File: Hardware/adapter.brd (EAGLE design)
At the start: 61.9 x 62.5 mm, 6 parts

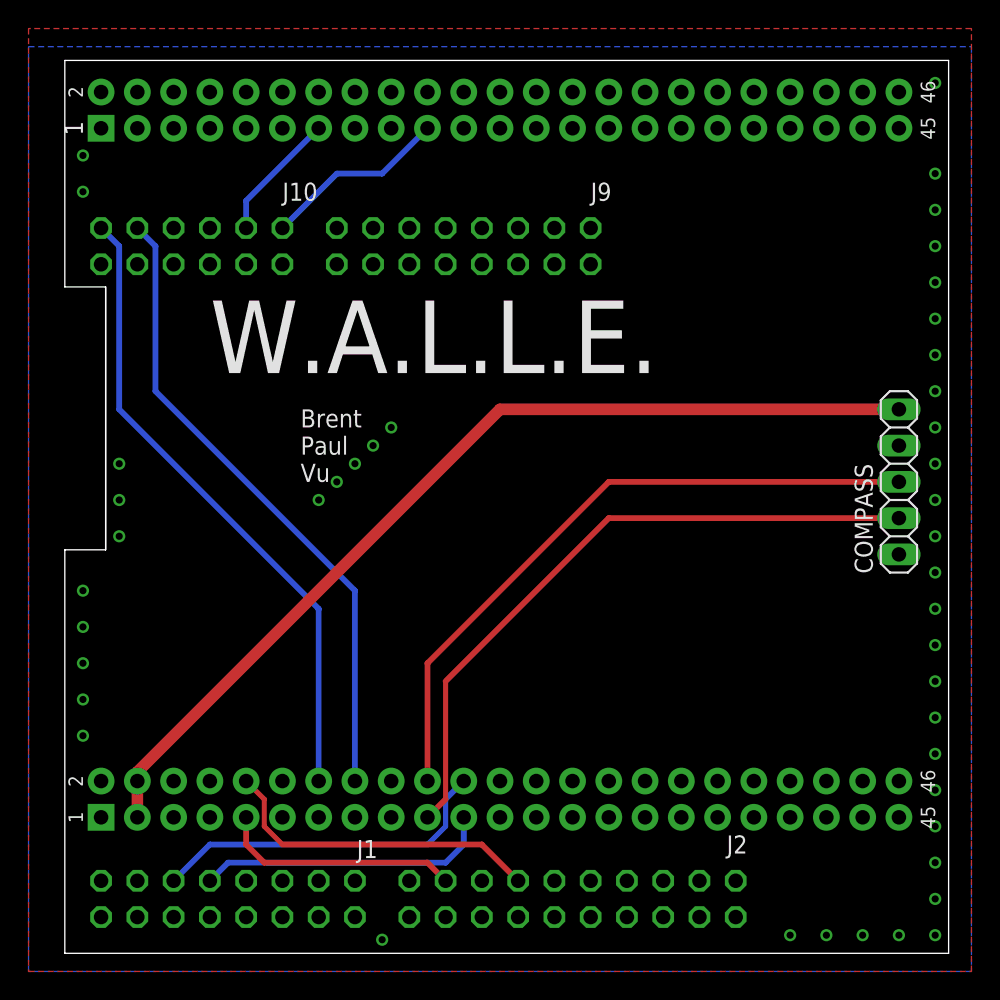
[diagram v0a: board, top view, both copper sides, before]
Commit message: Added GPIO connections for switches and LEDs. Updated routing.
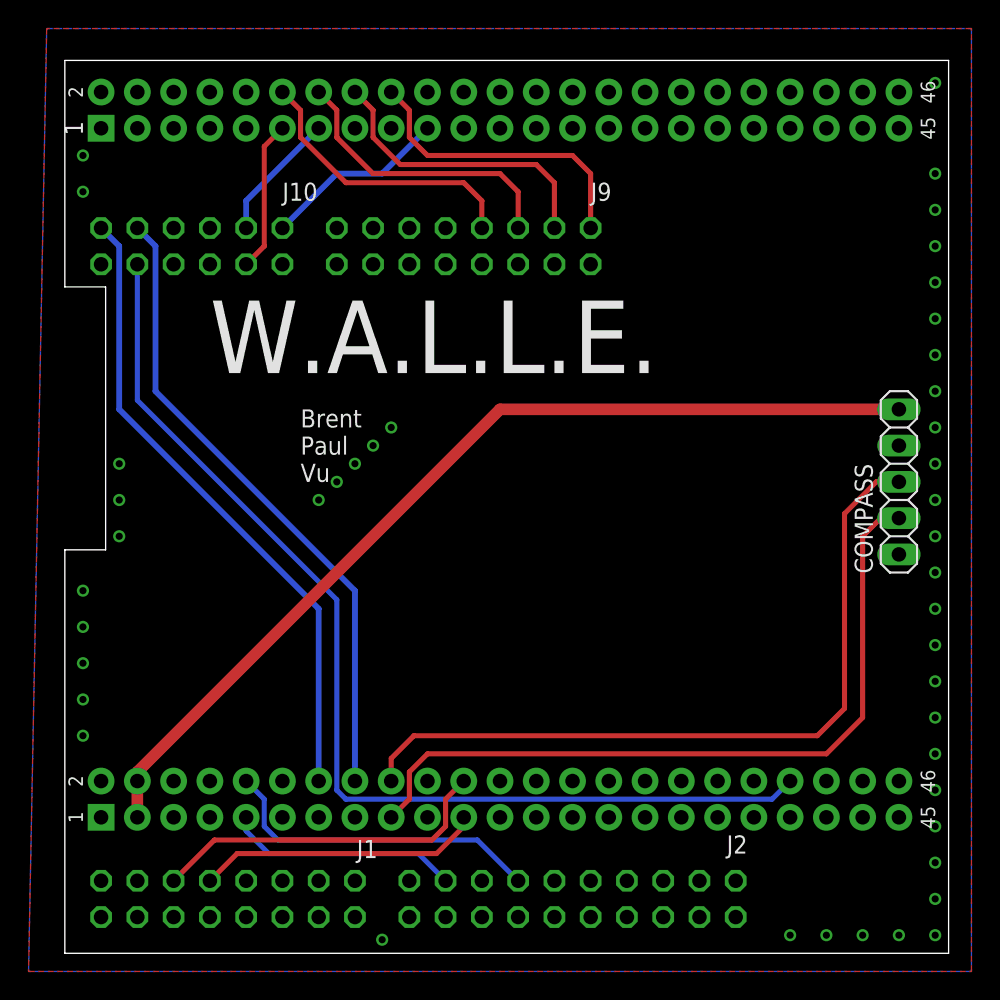
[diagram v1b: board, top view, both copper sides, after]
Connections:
- removed net N$1: COMPASS.2, U$1.P9.19
- removed net N$2: COMPASS.3, U$1.P9.20
- removed net N$3: J10.9
- removed net N$4: J10.3
- removed net N$5: J9.2
- removed net N$6: J9.4
- removed net N$7: J9.6
- removed net N$8: J9.8
- new net BATSENSE: J10.9, U$1.P9.40
- new net HB_EN: J10.3, U$1.P8.11
- new net I2C1_SCL: COMPASS.2, U$1.P9.17
- new net I2C1_SDA: COMPASS.3, U$1.P9.18
- new net LED1: J9.2, U$1.P8.18
- new net LED2: J9.4, U$1.P8.16
- new net LED3: J9.6, U$1.P8.14
- new net LED4: J9.8, U$1.P8.12
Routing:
- net BATSENSE: track 0.00 -> 75.2 mm
- net I2C1_SDA: track 0.00 -> 53.2 mm
- net I2C1_SCL: track 0.00 -> 52.8 mm
- net N$2: track 46.5 -> 0.00 mm
- net N$1: track 46.5 -> 0.00 mm
- net LED1: track 0.00 -> 21.3 mm
- net LED2: track 0.00 -> 20.9 mm
- net LED3: track 0.00 -> 20.5 mm
- net LED4: track 0.00 -> 20.1 mm
- net HB_EN: track 0.00 -> 10.6 mm
- net PWM0B: track 20.7 -> 20.0 mm
- net PWR_SW: track 16.9 -> 16.4 mm

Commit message: Updated board outline.
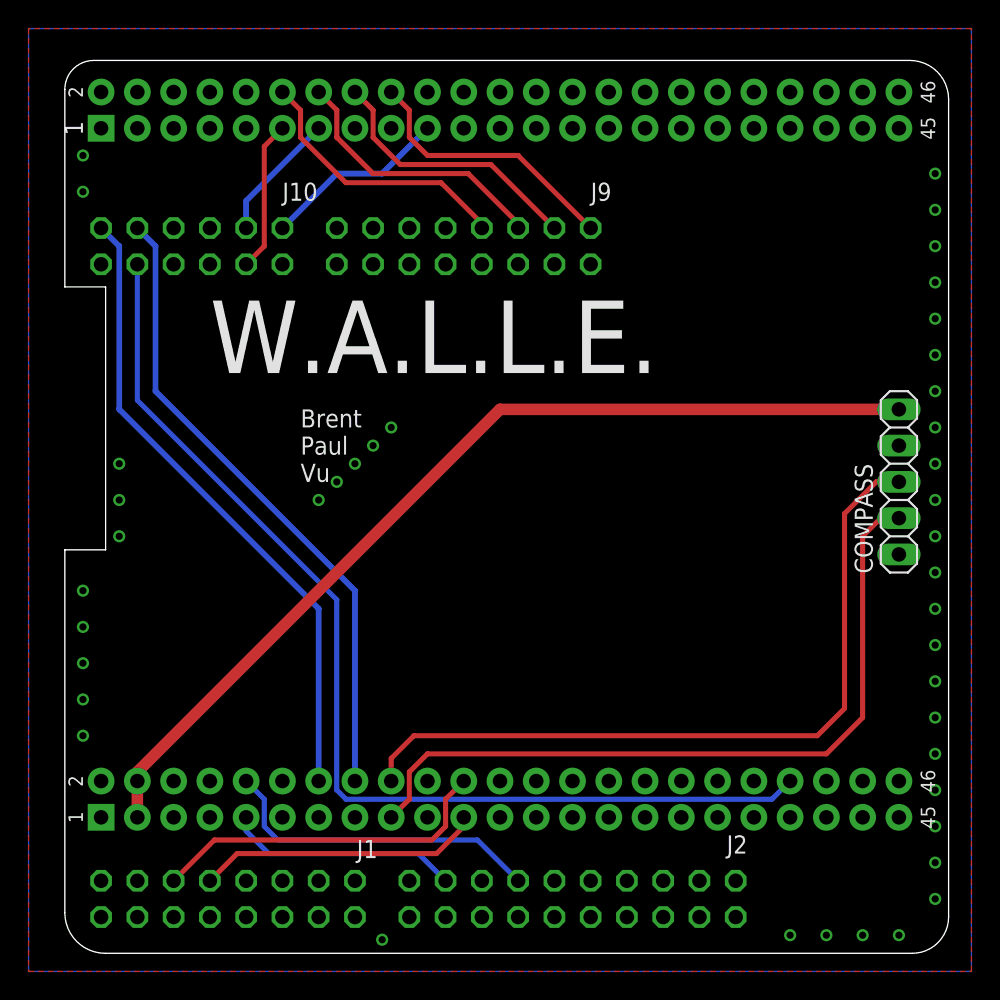
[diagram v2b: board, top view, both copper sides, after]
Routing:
- net LED1: track 21.3 -> 19.0 mm
- net LED2: track 20.9 -> 19.0 mm
- net LED3: track 20.5 -> 19.2 mm
- net LED4: track 20.1 -> 19.2 mm
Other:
- outline, holes or cut-outs redrawn
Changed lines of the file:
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@@
 <board>
 <plain>
-<wire x1="26.67" y1="1.27" x2="88.57" y2="1.27" width="0" layer="20"/>
-<wire x1="88.57" y1="1.27" x2="88.57" y2="63.8075" width="0" layer="20"/>
-<wire x1="88.57" y1="63.8075" x2="26.67" y2="63.8075" width="0" layer="20"/>
-<wire x1="26.67" y1="63.8075" x2="26.67" y2="47.9425" width="0" layer="20"/>
+<wire x1="26.67" y1="29.5275" x2="26.67" y2="4.10980625" width="0" layer="20"/>
+<wire x1="26.67" y1="4.10980625" x2="29.50980625" y2="1.27" width="0" layer="20" curve="90"/>
+<wire x1="29.50980625" y1="1.27" x2="86.02108125" y2="1.27" width="0" layer="20"/>
+<wire x1="86.02108125" y1="1.27" x2="88.57" y2="3.81891875" width="0" layer="20" curve="90"/>
+<wire x1="88.57" y1="3.81891875" x2="88.57" y2="61.092246875" width="0" layer="20"/>
+<wire x1="88.57" y1="61.092246875" x2="85.854746875" y2="63.8075" width="0" layer="20" curve="90"/>
+<wire x1="85.854746875" y1="63.8075" x2="28.695190625" y2="63.8075" width="0" layer="20"/>
+<wire x1="28.695190625" y1="63.8075" x2="26.67" y2="61.782309375" width="0" layer="20" curve="90"/>
+<wire x1="26.67" y1="61.782309375" x2="26.67" y2="47.9425" width="0" layer="20"/>
 <wire x1="26.67" y1="47.9425" x2="29.5275" y2="47.9425" width="0" layer="20"/>
 <wire x1="29.5275" y1="29.5275" x2="26.67" y2="29.5275" width="0" layer="20"/>
-<wire x1="26.67" y1="29.5275" x2="26.67" y2="1.27" width="0" layer="20"/>
 <text x="36.83" y="41.91" size="5.08" layer="21">W.A.L.L.E.</text>
 <text x="43.18" y="34.29" size="1.27" layer="21">Brent
@@
 <contactref element="J9" pad="13"/>
 <polygon width="0.4064" layer="1">
-<vertex x="25.4" y="66.04"/>
+<vertex x="24.13" y="66.04"/>
 <vertex x="24.13" y="0"/>
 <vertex x="90.17" y="0"/>
@@
 </polygon>
 <polygon width="0.4064" layer="16">
-<vertex x="25.4" y="66.04"/>
+<vertex x="24.13" y="66.04"/>
 <vertex x="90.17" y="66.04"/>
 <vertex x="90.17" y="0"/>
@@
 <via x="87.63" y="7.62" extent="1-16" drill="0.5"/>
 <via x="87.63" y="5.08" extent="1-16" drill="0.5"/>
-<via x="87.63" y="2.54" extent="1-16" drill="0.5"/>
+<wire x1="87.63" y1="2.54" x2="87.63" y2="2.54" width="0" layer="19" extent="1-16"/>
 <via x="85.09" y="2.54" extent="1-16" drill="0.5"/>
 <via x="82.55" y="2.54" extent="1-16" drill="0.5"/>
@@
 <via x="30.48" y="35.56" extent="1-16" drill="0.5"/>
 <via x="87.63" y="55.88" extent="1-16" drill="0.5"/>
-<via x="87.63" y="62.23" extent="1-16" drill="0.5"/>
+<wire x1="87.63" y1="62.23" x2="87.63" y2="62.23" width="0" layer="19" extent="1-16"/>
 <via x="27.94" y="54.61" extent="1-16" drill="0.5"/>
 <via x="27.94" y="57.15" extent="1-16" drill="0.5"/>
@@
 <contactref element="J9" pad="2"/>
 <contactref element="U$1" pad="P8.18"/>
-<wire x1="63.5" y1="52.07" x2="63.5" y2="55.88" width="0.3556" layer="1"/>
-<wire x1="62.23" y1="57.15" x2="52.07" y2="57.15" width="0.3556" layer="1"/>
 <wire x1="52.07" y1="57.15" x2="50.8" y2="58.42" width="0.3556" layer="1"/>
 <wire x1="50.8" y1="58.42" x2="50.8" y2="60.325" width="0.3556" layer="1"/>
 <wire x1="50.8" y1="60.325" x2="49.53" y2="61.595" width="0.3556" layer="1"/>
-<wire x1="63.5" y1="55.88" x2="62.23" y2="57.15" width="0.3556" layer="1"/>
+<wire x1="52.07" y1="57.15" x2="58.42" y2="57.15" width="0.3556" layer="1"/>
+<wire x1="58.42" y1="57.15" x2="63.5" y2="52.07" width="0.3556" layer="1"/>
 </signal>
 <signal name="LED2">
@@
 <wire x1="48.26" y1="58.42" x2="48.26" y2="60.325" width="0.3556" layer="1"/>
 <wire x1="48.26" y1="60.325" x2="46.99" y2="61.595" width="0.3556" layer="1"/>
-<wire x1="50.165" y1="56.515" x2="59.69" y2="56.515" width="0.3556" layer="1"/>
-<wire x1="59.69" y1="56.515" x2="60.96" y2="55.245" width="0.3556" layer="1"/>
-<wire x1="60.96" y1="55.245" x2="60.96" y2="52.07" width="0.3556" layer="1"/>
+<wire x1="60.96" y1="52.07" x2="56.515" y2="56.515" width="0.3556" layer="1"/>
+<wire x1="56.515" y1="56.515" x2="50.165" y2="56.515" width="0.3556" layer="1"/>
 </signal>
 <signal name="LED3">
@@
 <wire x1="45.72" y1="60.325" x2="45.72" y2="58.42" width="0.3556" layer="1"/>
 <wire x1="45.72" y1="58.42" x2="48.26" y2="55.88" width="0.3556" layer="1"/>
-<wire x1="48.26" y1="55.88" x2="57.15" y2="55.88" width="0.3556" layer="1"/>
-<wire x1="57.15" y1="55.88" x2="58.42" y2="54.61" width="0.3556" layer="1"/>
-<wire x1="58.42" y1="54.61" x2="58.42" y2="52.07" width="0.3556" layer="1"/>
+<wire x1="48.26" y1="55.88" x2="54.9275" y2="55.88" width="0.3556" layer="1"/>
+<wire x1="54.9275" y1="55.88" x2="58.42" y2="52.3875" width="0.3556" layer="1"/>
+<wire x1="58.42" y1="52.3875" x2="58.42" y2="52.07" width="0.3556" layer="1"/>
 </signal>
 <signal name="LED4">
 <contactref element="J9" pad="8"/>
 <contactref element="U$1" pad="P8.12"/>
-<wire x1="55.88" y1="52.07" x2="55.88" y2="53.975" width="0.3556" layer="1"/>
-<wire x1="54.61" y1="55.245" x2="46.355" y2="55.245" width="0.3556" layer="1"/>
 <wire x1="46.355" y1="55.245" x2="43.18" y2="58.42" width="0.3556" layer="1"/>
 <wire x1="43.18" y1="58.42" x2="43.18" y2="60.325" width="0.3556" layer="1"/>
 <wire x1="43.18" y1="60.325" x2="41.91" y2="61.595" width="0.3556" layer="1"/>
-<wire x1="54.61" y1="55.245" x2="55.88" y2="53.975" width="0.3556" layer="1"/>
+<wire x1="55.88" y1="52.07" x2="55.88" y2="52.3875" width="0.3556" layer="1"/>
+<wire x1="55.88" y1="52.3875" x2="53.0225" y2="55.245" width="0.3556" layer="1"/>
+<wire x1="53.0225" y1="55.245" x2="46.355" y2="55.245" width="0.3556" layer="1"/>
 </signal>
 </signals>

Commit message: Added 5V regulator. Fixed J9 flip issue.
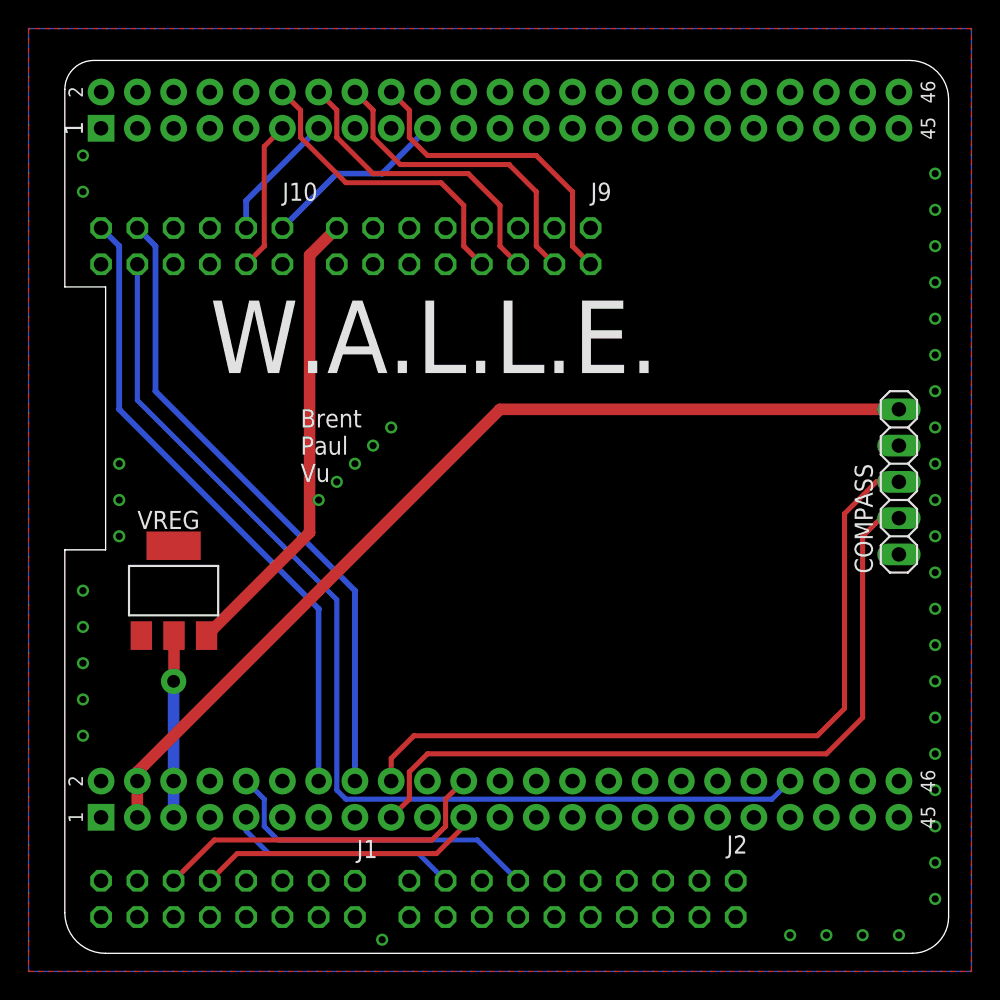
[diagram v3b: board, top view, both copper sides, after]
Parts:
- added VREG: REG1117, burr-brown:SOT223
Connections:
- new net 5V: U$1.P9.5, U$1.P9.6, VREG.2
- new net VBAT: J9.16, VREG.3
- net GND: now also J9.12, J9.14, VREG.1; no longer J9.11, J9.13
- net LED1: now also J9.1; no longer J9.2
- net LED2: now also J9.3; no longer J9.4
- net LED3: now also J9.5; no longer J9.6
- net LED4: now also J9.7; no longer J9.8
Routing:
- net VBAT: track 0.00 -> 32.3 mm
- net 5V: track 0.00 -> 12.7 mm, vias 0 -> 1
- net LED2: track 19.0 -> 22.3 mm
- net LED1: track 19.0 -> 22.3 mm
- net LED4: track 19.2 -> 21.8 mm
- net LED3: track 19.2 -> 21.8 mm
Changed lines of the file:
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@@
 <attribute name="VALUE" x="64.77" y="46.355" size="1.27" layer="28" rot="MR0"/>
+</element>
+<element name="VREG" library="burr-brown" package="SOT223" value="REG1117" x="34.29" y="26.67">
+<attribute name="OC_NEWARK" value="14P6981" x="34.29" y="26.67" size="1.778" layer="27" display="off"/>
+<attribute name="MPN" value="REG1117" x="34.29" y="26.67" size="1.778" layer="27" display="off"/>
+<attribute name="MF" value="" x="34.29" y="26.67" size="1.778" layer="27" display="off"/>
+<attribute name="OC_FARNELL" value="1097566" x="34.29" y="26.67" size="1.778" layer="27" display="off"/>
 </element>
 </elements>
@@
 <contactref element="U$1" pad="P8.1"/>
 <contactref element="U$1" pad="P8.2"/>
-<contactref element="J9" pad="11"/>
-<contactref element="J9" pad="13"/>
 <polygon width="0.4064" layer="1">
 <vertex x="24.13" y="66.04"/>
@@
 <via x="87.63" y="7.62" extent="1-16" drill="0.5"/>
 <via x="87.63" y="5.08" extent="1-16" drill="0.5"/>
-<wire x1="87.63" y1="2.54" x2="87.63" y2="2.54" width="0" layer="19" extent="1-16"/>
 <via x="85.09" y="2.54" extent="1-16" drill="0.5"/>
 <via x="82.55" y="2.54" extent="1-16" drill="0.5"/>
@@
 <via x="30.48" y="35.56" extent="1-16" drill="0.5"/>
 <via x="87.63" y="55.88" extent="1-16" drill="0.5"/>
-<wire x1="87.63" y1="62.23" x2="87.63" y2="62.23" width="0" layer="19" extent="1-16"/>
 <via x="27.94" y="54.61" extent="1-16" drill="0.5"/>
 <via x="27.94" y="57.15" extent="1-16" drill="0.5"/>
@@
 <via x="48.26" y="36.83" extent="1-16" drill="0.5"/>
 <via x="49.53" y="38.1" extent="1-16" drill="0.5"/>
+<contactref element="VREG" pad="1"/>
+<contactref element="J9" pad="14"/>
+<contactref element="J9" pad="12"/>
 </signal>
 <signal name="I2C1_SCL">
@@
 </signal>
 <signal name="LED1">
-<contactref element="J9" pad="2"/>
 <contactref element="U$1" pad="P8.18"/>
 <wire x1="52.07" y1="57.15" x2="50.8" y2="58.42" width="0.3556" layer="1"/>
 <wire x1="50.8" y1="58.42" x2="50.8" y2="60.325" width="0.3556" layer="1"/>
 <wire x1="50.8" y1="60.325" x2="49.53" y2="61.595" width="0.3556" layer="1"/>
-<wire x1="52.07" y1="57.15" x2="58.42" y2="57.15" width="0.3556" layer="1"/>
-<wire x1="58.42" y1="57.15" x2="63.5" y2="52.07" width="0.3556" layer="1"/>
+<wire x1="52.07" y1="57.15" x2="59.69" y2="57.15" width="0.3556" layer="1"/>
+<contactref element="J9" pad="1"/>
+<wire x1="63.5" y1="49.53" x2="62.23" y2="50.8" width="0.3556" layer="1"/>
+<wire x1="62.23" y1="50.8" x2="62.23" y2="54.61" width="0.3556" layer="1"/>
+<wire x1="62.23" y1="54.61" x2="59.69" y2="57.15" width="0.3556" layer="1"/>
 </signal>
 <signal name="LED2">
-<contactref element="J9" pad="4"/>
 <contactref element="U$1" pad="P8.16"/>
 <wire x1="50.165" y1="56.515" x2="48.26" y2="58.42" width="0.3556" layer="1"/>
 <wire x1="48.26" y1="58.42" x2="48.26" y2="60.325" width="0.3556" layer="1"/>
 <wire x1="48.26" y1="60.325" x2="46.99" y2="61.595" width="0.3556" layer="1"/>
-<wire x1="60.96" y1="52.07" x2="56.515" y2="56.515" width="0.3556" layer="1"/>
-<wire x1="56.515" y1="56.515" x2="50.165" y2="56.515" width="0.3556" layer="1"/>
+<wire x1="57.785" y1="56.515" x2="50.165" y2="56.515" width="0.3556" layer="1"/>
+<contactref element="J9" pad="3"/>
+<wire x1="60.96" y1="49.53" x2="59.69" y2="50.8" width="0.3556" layer="1"/>
+<wire x1="59.69" y1="50.8" x2="59.69" y2="54.61" width="0.3556" layer="1"/>
+<wire x1="59.69" y1="54.61" x2="57.785" y2="56.515" width="0.3556" layer="1"/>
 </signal>
 <signal name="LED3">
-<contactref element="J9" pad="6"/>
 <contactref element="U$1" pad="P8.14"/>
 <wire x1="44.45" y1="61.595" x2="45.72" y2="60.325" width="0.3556" layer="1"/>
@@
 <wire x1="45.72" y1="58.42" x2="48.26" y2="55.88" width="0.3556" layer="1"/>
 <wire x1="48.26" y1="55.88" x2="54.9275" y2="55.88" width="0.3556" layer="1"/>
-<wire x1="54.9275" y1="55.88" x2="58.42" y2="52.3875" width="0.3556" layer="1"/>
-<wire x1="58.42" y1="52.3875" x2="58.42" y2="52.07" width="0.3556" layer="1"/>
+<contactref element="J9" pad="5"/>
+<wire x1="58.42" y1="49.53" x2="57.15" y2="50.8" width="0.3556" layer="1"/>
+<wire x1="57.15" y1="50.8" x2="57.15" y2="53.6575" width="0.3556" layer="1"/>
+<wire x1="57.15" y1="53.6575" x2="54.9275" y2="55.88" width="0.3556" layer="1"/>
 </signal>
 <signal name="LED4">
-<contactref element="J9" pad="8"/>
 <contactref element="U$1" pad="P8.12"/>
 <wire x1="46.355" y1="55.245" x2="43.18" y2="58.42" width="0.3556" layer="1"/>
 <wire x1="43.18" y1="58.42" x2="43.18" y2="60.325" width="0.3556" layer="1"/>
 <wire x1="43.18" y1="60.325" x2="41.91" y2="61.595" width="0.3556" layer="1"/>
-<wire x1="55.88" y1="52.07" x2="55.88" y2="52.3875" width="0.3556" layer="1"/>
-<wire x1="55.88" y1="52.3875" x2="53.0225" y2="55.245" width="0.3556" layer="1"/>
 <wire x1="53.0225" y1="55.245" x2="46.355" y2="55.245" width="0.3556" layer="1"/>
+<contactref element="J9" pad="7"/>
+<wire x1="55.88" y1="49.53" x2="54.61" y2="50.8" width="0.3556" layer="1"/>
+<wire x1="54.61" y1="50.8" x2="54.61" y2="53.6575" width="0.3556" layer="1"/>
+<wire x1="54.61" y1="53.6575" x2="53.0225" y2="55.245" width="0.3556" layer="1"/>
+</signal>
+<signal name="VBAT">
+<contactref element="VREG" pad="3"/>
+<contactref element="J9" pad="16"/>
+<wire x1="36.6014" y1="23.5204" x2="43.815" y2="30.734" width="0.8128" layer="1"/>
+<wire x1="43.815" y1="30.734" x2="43.815" y2="50.165" width="0.8128" layer="1"/>
+<wire x1="43.815" y1="50.165" x2="45.72" y2="52.07" width="0.8128" layer="1"/>
+</signal>
+<signal name="5V">
+<contactref element="VREG" pad="2"/>
+<contactref element="U$1" pad="P9.6"/>
+<contactref element="U$1" pad="P9.5"/>
+<wire x1="34.29" y1="10.795" x2="34.29" y2="13.335" width="0.8128" layer="16"/>
+<wire x1="34.29" y1="13.335" x2="34.29" y2="20.32" width="0.8128" layer="16"/>
+<wire x1="34.3154" y1="23.5204" x2="34.3154" y2="20.3454" width="0.8128" layer="1"/>
+<wire x1="34.3154" y1="20.3454" x2="34.29" y2="20.32" width="0.8128" layer="1"/>
+<via x="34.29" y="20.32" extent="1-16" drill="0.9" diameter="1.778"/>
 </signal>
 </signals>
